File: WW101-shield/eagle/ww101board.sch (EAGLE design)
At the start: 57 parts

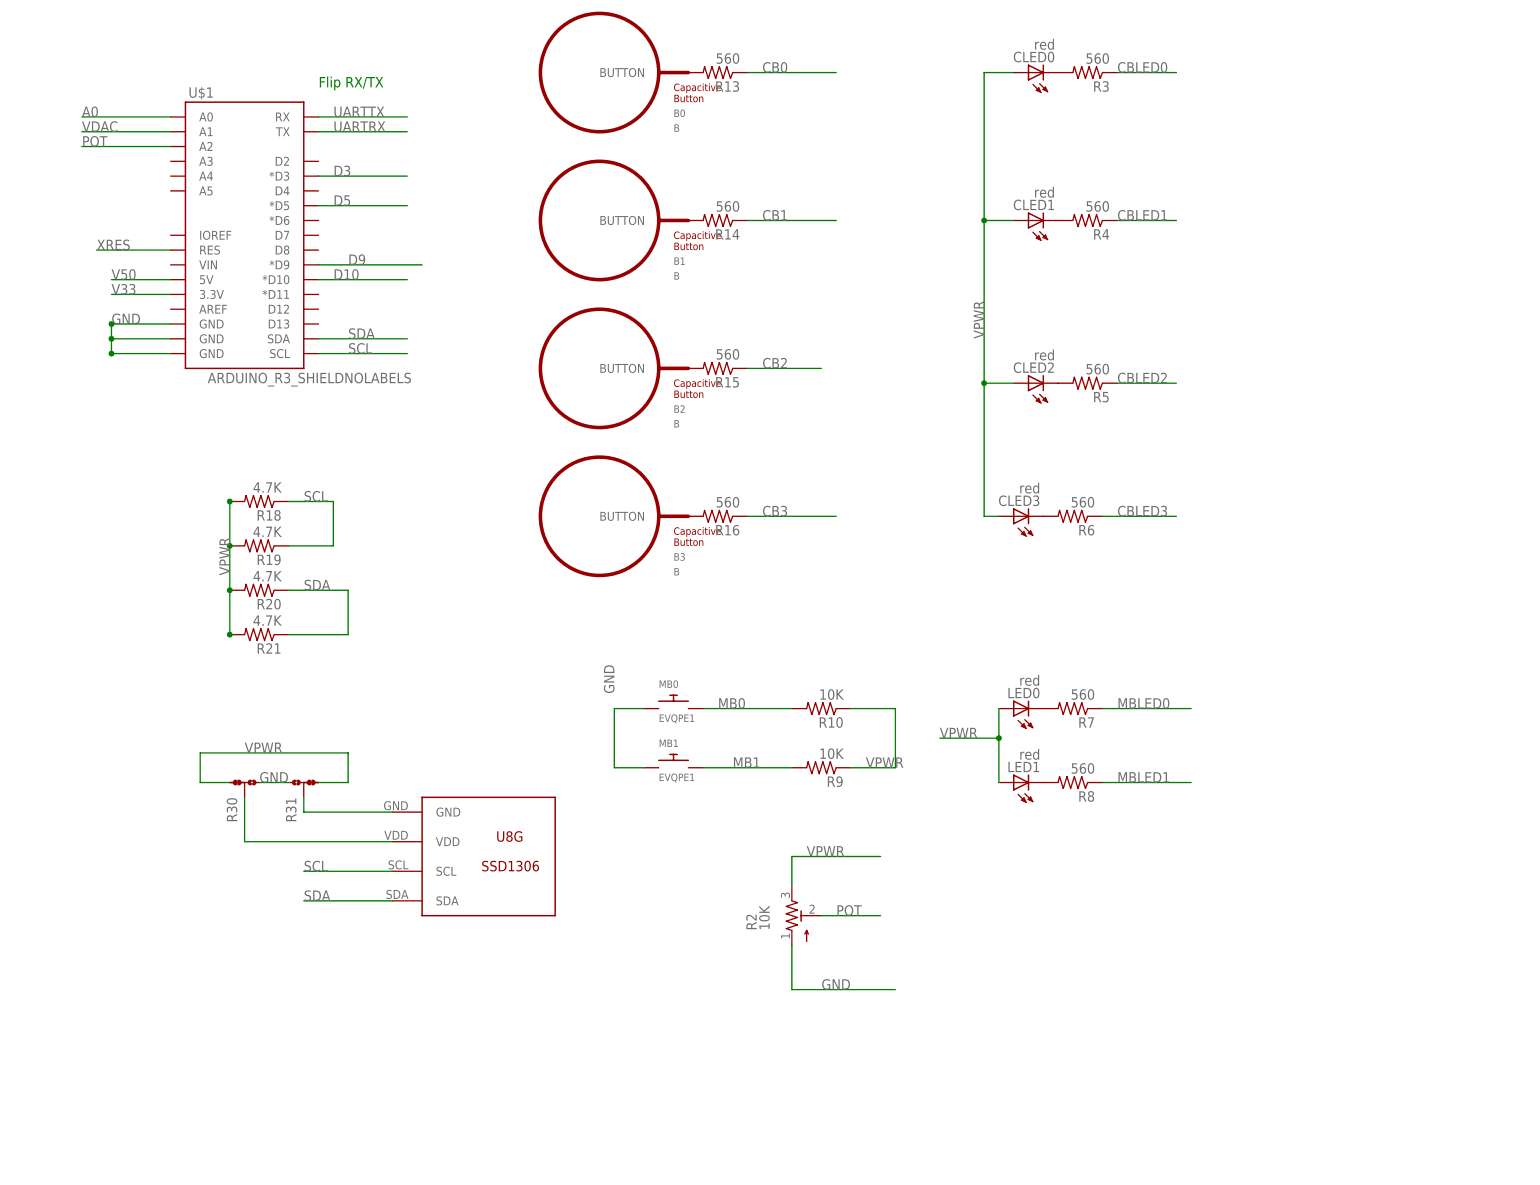
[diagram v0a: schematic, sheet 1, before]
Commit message: Updated to latest board files and remove u8g lib from upper level.
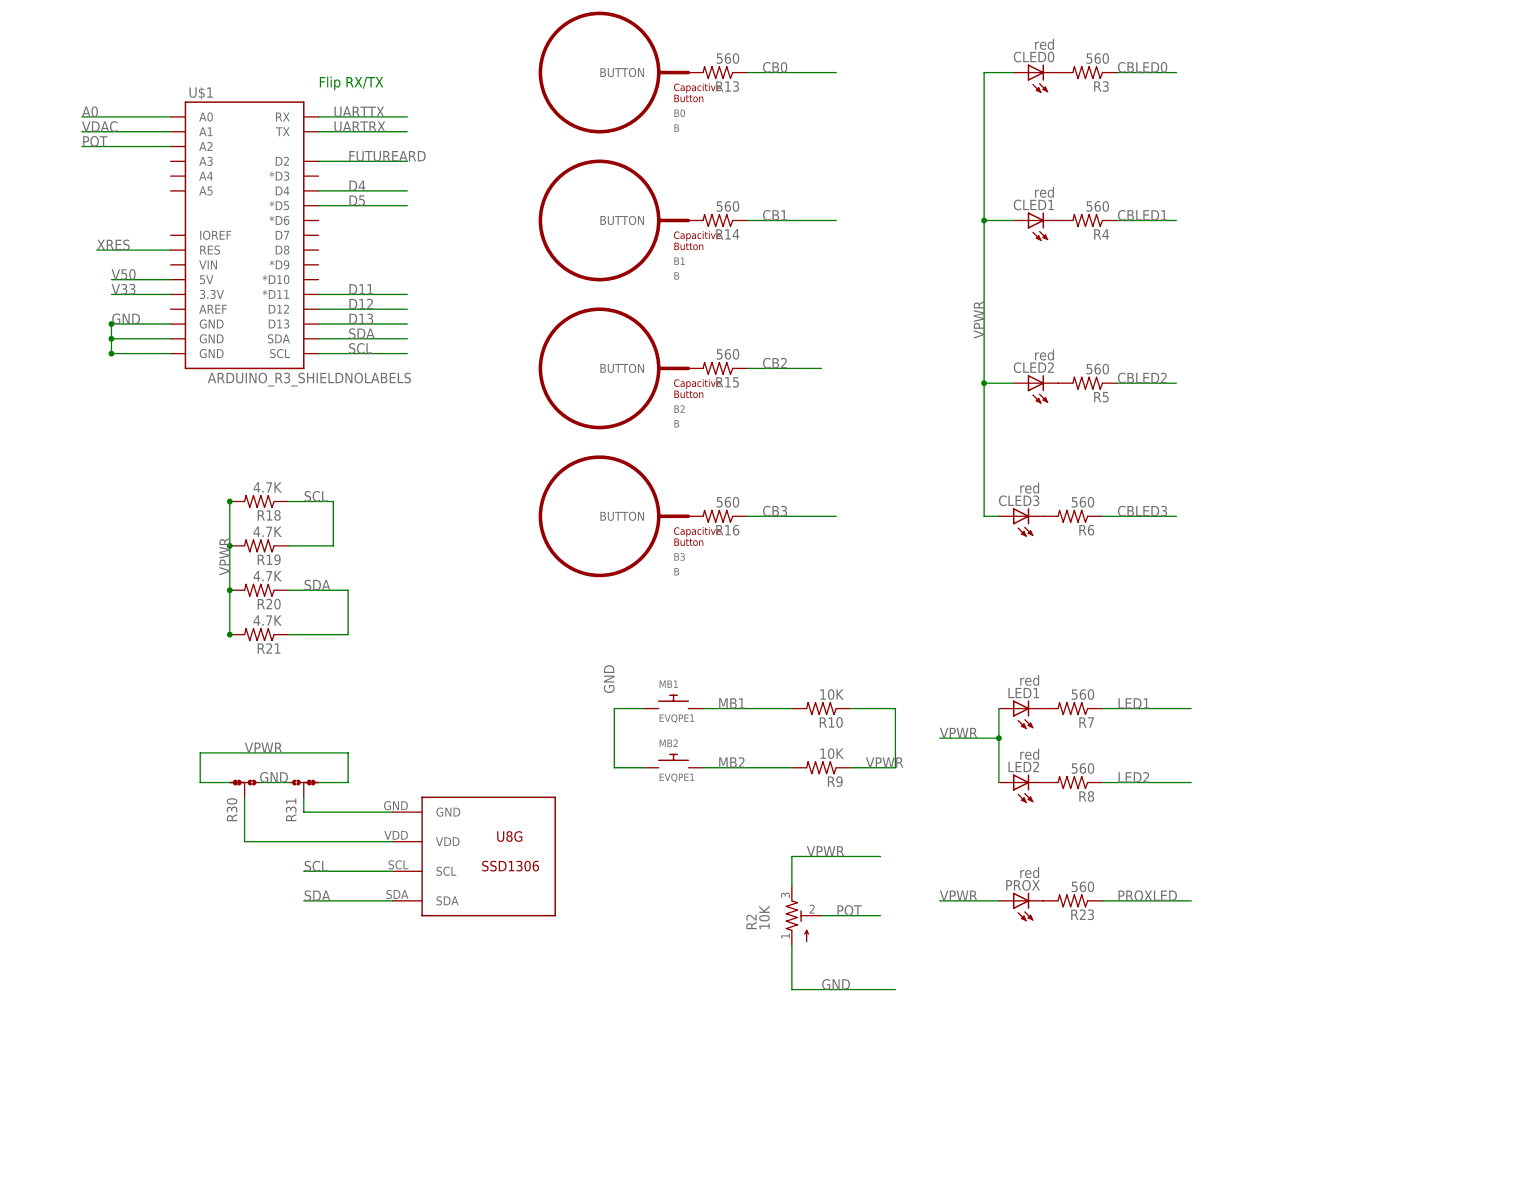
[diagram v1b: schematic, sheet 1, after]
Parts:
- removed LED0: red, adafruit:LEDCHIP-LED0603
- removed MB0: EVQPE1, IOTExpert:EVQPE1
- added LED2, PROX: red, adafruit:LEDCHIP-LED0603
- added MB2: EVQPE1, IOTExpert:EVQPE1
- added R22: 10K, PatternAgents-ProtoPads:RESISTOR0603
- added R23: 560, PatternAgents-ProtoPads:RESISTOR0603
- added R24: 0R, PatternAgents-ProtoPads:RESISTOR0603
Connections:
- net MBLED1 renamed LED2
- removed net D10: U$1.*D10, U$7.P0[7]
- removed net D3: U$1.*D3, U$7.P0[3]
- removed net D9: U$1.*D9, U$7.P0[6]
- removed net MB0: JP1.2, MB0.P$2, R10.2, U$7.P0[1]
- removed net MBLED0: R7.1, U$7.P0[2]
- new net CMESH: R24.1
- new net D11: U$1.*D11, U$7.P0[7]
- new net D12: U$1.D12, U$7.P0[2]
- new net D13: U$1.D13, U$7.P3[1]
- new net D4: U$1.D4, U$7.P0[3]
- new net FUTUREARD: U$1.D2, U$7.P3[2]
- new net LED1: R7.1, U$7.P0[6]
- new net MB2: JP1.2, MB2.P$2, R9.2, U$7.P0[1]
- new net N$3: PROX.C, R23.2
- new net PROXLED: R23.1, U$7.P3[0]
- net CSHIELD: now also R24.2
- net GND: now also MB2.P$1; no longer MB0.P$1
- net MB1: now also R10.2; no longer R9.2
- net N$12: now also LED1.C; no longer LED0.C
- net N$13: now also LED2.C; no longer LED1.C
- net VPWR: now also LED2.A, PROX.A, R22.1; no longer LED0.A
- net XRES: now also R22.2
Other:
- note added: "1%"
- note added: "SCLK"
- note added: "SDAT"
- moved on the sheet: LED1, MB1

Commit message: Move cap on XRES to gnd, make holes larger for OLED and humidity sensor.
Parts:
- removed JMP1: 0, PatternAgents-ProtoPads:JMP-3-NO-PTH
- removed JP1: 0, SparkFun-Connectors:M05LOCK
- removed JPWR: 0, PatternAgents-ProtoPads:JMP-3-NO-0603
- removed U$2: U8G-096-OLED, IOTExpert:U8G-096-OLED
- added C15, C16: 0.1uF, ww101board:CAP0603-CAP
- added C17: 10uF, ww101board:CAP0603-CAP
- added J5: (no value), ww101board:JMP-3-PTH-PTH
- added J6: U8G-096-OLED, ww101board:U8G-096-OLED
- added J7: 0, ww101board:M05LOCK
- added R25: 0R, ww101board:RESISTOR0603
- added R26, R27: 50K, ww101board:RESISTOR0603
- added R32: (no value), ww101board:JMP-3-NO
- added U7: CY8C4A45-48, ww101board:CY8C4A45-48
- B0, B1, B2, B3: device PatternAgents-TouchWidgets:BUTTON_PASSIVE10MM -> ww101board:BUTTON_PASSIVE10MM
- C1, C10, C11, C12, C13, C14, C2, C3, C4, C5, C6, C7, C8, C9: device PatternAgents-ProtoPads:CAP0603-CAP -> ww101board:CAP0603-CAP
- CLED0, CLED1, CLED2, CLED3, LED1, LED2, PROX: device adafruit:LEDCHIP-LED0603 -> ww101board:LEDCHIP-LED0603
- D1: device IOTExpert:ALS -> ww101board:ALS
- HUMIDITY: device IOTExpert:HPP801A031 -> ww101board:HPP801A031
- MB1, MB2: device IOTExpert:EVQPE1 -> ww101board:EVQPE1
- R1, R10, R12, R13, R14, R15, R16, R17, R22, R23, R24, R3, R4, R5, R6, R7, R8, R9: device PatternAgents-ProtoPads:RESISTOR0603 -> ww101board:RESISTOR0603
- R11: device varistor:THERMISTOR-5 -> ww101board:THERMISTOR-5
- R18, R19, R20, R21: value 4.7K -> DNP; device PatternAgents-ProtoPads:RESISTOR0603 -> ww101board:RESISTOR0603
- R2: device pot:TRIM_US-3386P -> ww101board:TRIM_US-3386P
- R30: device PatternAgents-ProtoPads:JMP-3-1_2 -> ww101board:JMP-3-1_2
- R31: device PatternAgents-ProtoPads:JMP-3-2_3 -> ww101board:JMP-3-2_3
- U$1: device SparkFun-Boards:ARDUINO_R3_SHIELDNOLABELS -> ww101board:ARDUINO_R3_SHIELDNOLABELS
- U$7: value CY8C4A45-48 -> CYLOGO-SILK; device PatternAgents-Cypress:CY8C4A45-48 -> ww101board:CYLOGO-SILK
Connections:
- removed net VPWR: C1.2, C2.2, C3.2, C4.2, C5.1, C6.1, C8.2, C9.2, CLED0.A, CLED1.A, CLED2.A, CLED3.A, D1.E1, JMP1.2, JP1.5, JPWR.2, LED1.A, LED2.A, PROX.A, R10.1, R18.2, R19.2, R2.3, R20.2, R21.2, R22.1, R30.1, R31.3, R9.1, U$7.VDDA1, U$7.VDDA2, U$7.VDDA3, U$7.VDDD
- new net CAP-PSOC: R25.2, U7.P2[5]
- new net VCC: C1.2, C17.1, C2.2, C3.2, C4.2, C5.1, C6.1, C8.2, C9.2, CLED0.A, CLED1.A, CLED2.A, CLED3.A, D1.E1, J5.2, J7.5, LED1.A, LED2.A, PROX.A, R10.1, R18.2, R19.2, R2.3, R20.2, R21.2, R22.1, R30.1, R31.3, R32.2, R9.1, U7.VDDA1, U7.VDDA2, U7.VDDA3, U7.VDDD
- net CAP-PROX: now also R25.1; no longer U$7.P2[5]
- net CB0: now also U7.P5[0]; no longer U$7.P5[0]
- net CB1: now also U7.P5[1]; no longer U$7.P5[1]
- net CB2: now also U7.P1[7]; no longer U$7.P1[7]
- net CB3: now also U7.P1[4]; no longer U$7.P1[4]
- net CBLED0: now also U7.P1[6]; no longer U$7.P1[6]
- net CBLED1: now also U7.P1[5]; no longer U$7.P1[5]
- net CBLED2: now also U7.P2[0]; no longer U$7.P2[0]
- net CBLED3: now also U7.P2[6]; no longer U$7.P2[6]
- net CMOD: now also U7.P5[2]; no longer U$7.P5[2]
- net CSHIELD: now also U7.P3[3]; no longer U$7.P3[3]
- net CTANK: now also U7.P5[3]; no longer U$7.P5[3]
- net D11: now also R27.2, U7.P0[7]; no longer U$7.P0[7]
- net D12: now also U7.P0[2]; no longer U$7.P0[2]
- net D13: now also U7.P3[1]; no longer U$7.P3[1]
- net D4: now also U7.P0[3]; no longer U$7.P0[3]
- net D5: now also R26.2, U7.P0[5]; no longer U$7.P0[5]
- net FUTUREARD: now also U7.P3[2]; no longer U$7.P3[2]
- net GND: now also C15.1, C16.2, C17.2, J7.4, R26.1, R27.1, U7.P3[7], U7.VSSA1, U7.VSSA2, U7.VSSA3, U7.VSSD; no longer JP1.4, U$7.P3[7], U$7.VSSA1, U$7.VSSA2, U$7.VSSA3, U$7.VSSD
- net H-REF-CAP: now also U7.P2[4]; no longer U$7.P2[4]
- net HUMIDITY: now also U7.P2[3]; no longer U$7.P2[3]
- net LED1: now also U7.P0[6]; no longer U$7.P0[6]
- net LED2: now also U7.P0[4]; no longer U$7.P0[4]
- net MB1: now also J7.1, U7.P0[0]; no longer JP1.1, U$7.P0[0]
- net MB2: now also J7.2, U7.P0[1]; no longer JP1.2, U$7.P0[1]
- net N$14: now also J6.VDD; no longer U$2.VDD
- net N$17: now also J6.GND; no longer U$2.GND
- net N$20: now also U7.VCCD; no longer U$7.VCCD
- net POT: now also C16.1, U7.P3[4]; no longer U$7.P3[4]
- net PROXLED: now also U7.P3[0]; no longer U$7.P3[0]
- net SCL: now also J6.SCL, U7.P4[0]; no longer U$2.SCL, U$7.P4[0]
- net SDA: now also J6.SDA, U7.P4[1]; no longer U$2.SDA, U$7.P4[1]
- net THERM-MID: now also U7.P3[5]; no longer U$7.P3[5]
- net THERM-REF-HIGH: now also U7.P1[3], U7.P3[6]; no longer U$7.P1[3], U$7.P3[6]
- net TIA_IN: now also U7.P2[1]; no longer U$7.P2[1]
- net TIA_OUT: now also U7.P2[2]; no longer U$7.P2[2]
- net UARTRX: now also U7.P1[0]; no longer U$7.P1[1]
- net UARTTX: now also U7.P1[1]; no longer U$7.P1[0]
- net V33: now also J5.3, R32.1; no longer JMP1.3, JPWR.3
- net V50: now also J5.1, R32.3; no longer JMP1.1, JPWR.1
- net VDAC: now also U7.P1[2]; no longer U$7.P1[2]
- net VREF: now also U7.P2[7]; no longer U$7.P2[7]
- net XRES: now also C15.2, J7.3, U7.XRES; no longer JP1.3, U$7.XRES
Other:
- note added: "10K"
- note added: "2.1"
- note added: "CY8C4247AZI-M485"
- note added: "CY8CKIT-032"
- note added: "DNP - J5 It will only be used in the situation where the user has to switch back and forth between v50 and v33 If that is required they will hand solder a header into the board and remove the 0ohm resistor from R32"
- note added: "J6"
- note added: "P37 should be a direct path to thermistor ground"
- note added: "PSoC"
- note added: "Power"
- note added: "R26/R27 make this look like a "real" LED"
- note added: "R32 is a 0 OHM resistor used to select the power supply Please solder a 0 ohm into the 3.3V default position"
- note added: "Sensors"
- note added: "The OLED Screen vendors sometimes have gnd/power and sometimes have power/gnd. R30 & R31 are 0 Ohm resistors on the top of the board that let you select the screen type When assembling make sure you put them in the right place or they will be hard to fix!!"
- note added: "Two sets of I2C Resistors (Top/Bottom) No Load - Only for base boards with no I2C resitors preinstalled on I2C"
- note added: "U7"
- note added: "User Interface"
